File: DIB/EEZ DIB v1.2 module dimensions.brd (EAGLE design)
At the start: 185 x 95 mm, 4 parts, among them X1 77317-104-28LF, X2 ZL263-20DG

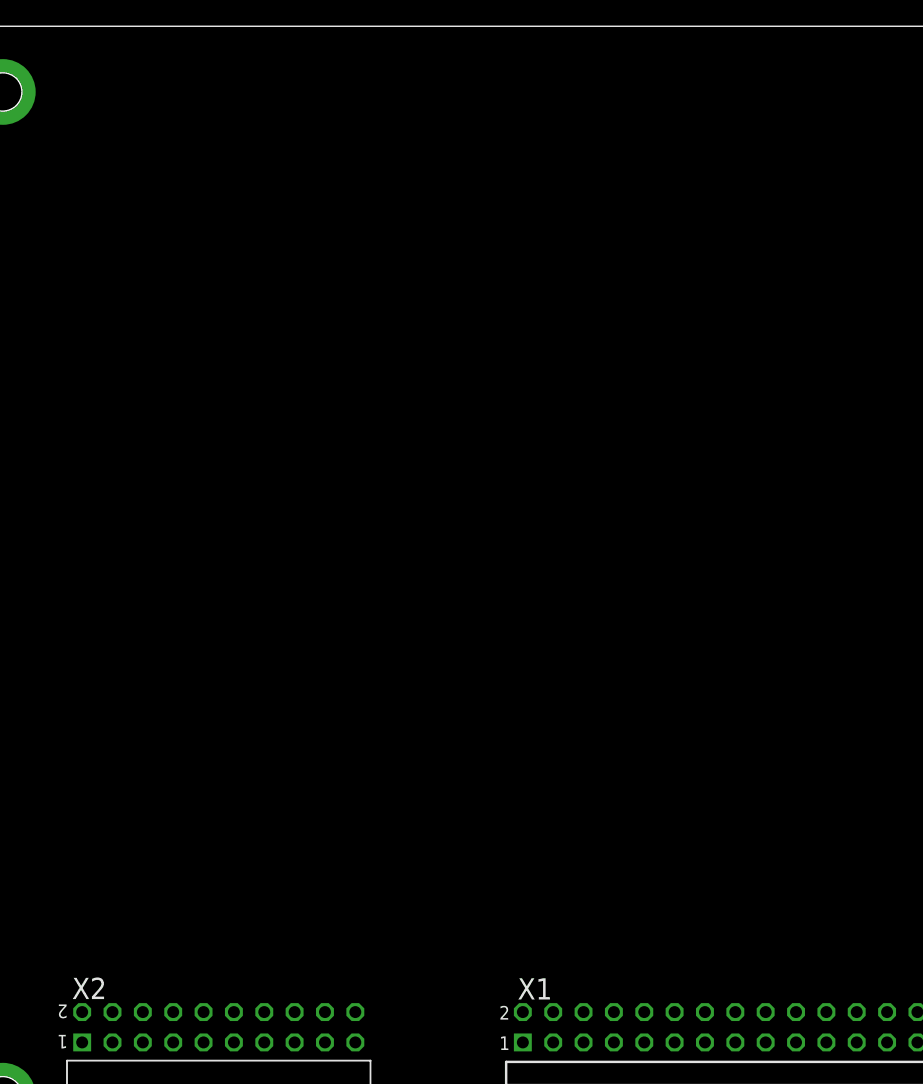
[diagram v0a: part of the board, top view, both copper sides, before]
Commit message: DIB v1.2 specification (ADIB added)
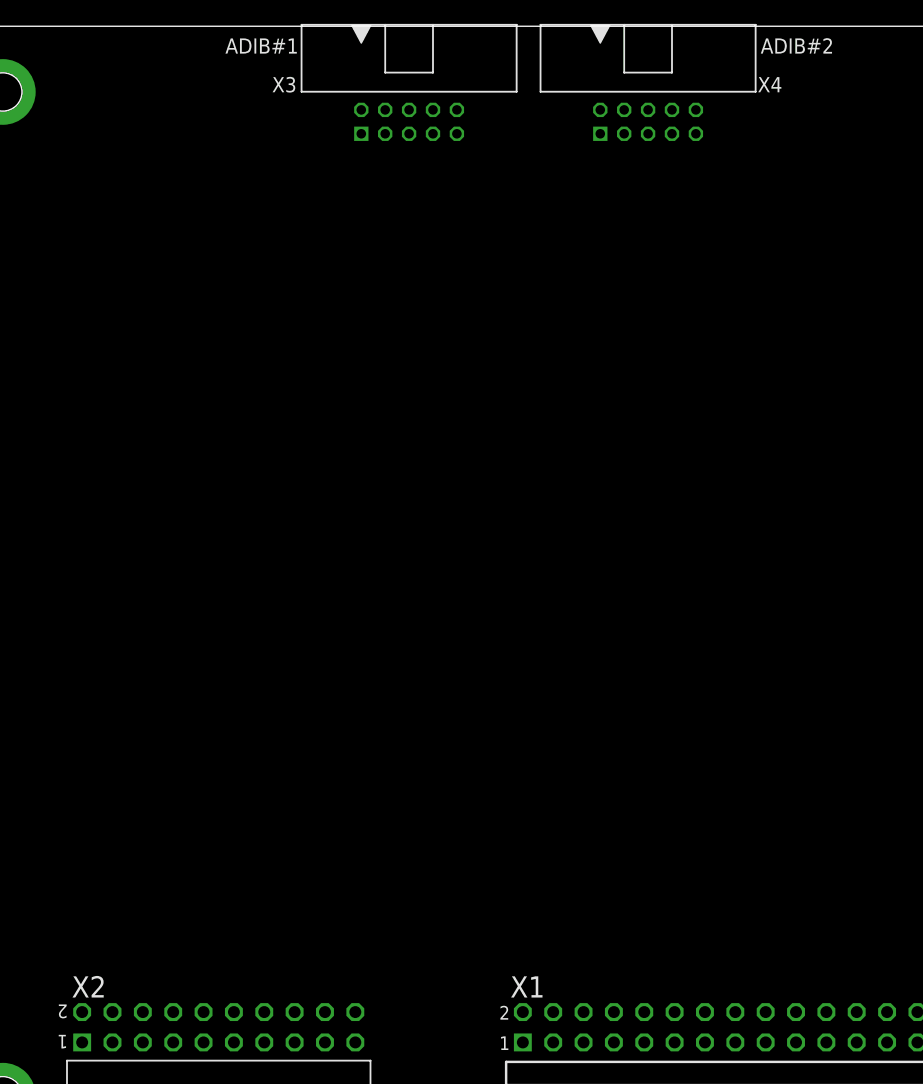
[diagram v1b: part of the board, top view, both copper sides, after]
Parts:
- added X3, X4: DS1014-10RF1B, EEZ_connectors:DS1014-10RF1B
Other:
- board text added: "ADIB#1"
- board text added: "ADIB#2"
- board text added: "Restricted area (DIB v1.2 and future expansion)"
- board text removed: "+48 Vdc"
- board text removed: "EEZ DIB ??? Project source code: github.com/eez-open"
- board text removed: "PE"
- board text removed: "Restricted area (DIB v1.0 and future expansion)"
